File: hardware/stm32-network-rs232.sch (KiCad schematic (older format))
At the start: 57 parts, among them J1 USB, M1 Mount Hole, M2 Mount Hole, M3 Mount Hole, M4 Mount Hole, P1 BELFUSE-08B0-1X1T-06-F, P2 P10, P3 DEBUG, P4 SWD, P5 RS232-TAP, P6 RS-232-DB-9-DTE, U1 ENC28J60, U2 STM32-48PIN, U3 MAX3221, U4 MOSFET-P, X1 25MHz, X2 8MHz

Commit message: more mods
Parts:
- C25: renamed from C?; value CP -> 10uF
- gave numbers to parts that had none: 1
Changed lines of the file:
@@
 USBDM
 $Comp
-L +3.3V #PWR31
+L +3.3V #PWR35
 U 1 1 53B60338
 P 9800 3000
-F 0 "#PWR31" H 9800 3090 20  0001 C CNN
+F 0 "#PWR35" H 9800 3090 20  0001 C CNN
 F 1 "+3.3V" H 9800 3090 30  0000 C CNN
 F 2 "" H 9800 3000 60  0000 C CNN
@@
 $EndComp
 $Comp
-L GNDPWR #PWR32
+L GNDPWR #PWR36
 U 1 1 53B603BB
 P 9800 3600
-F 0 "#PWR32" H 9800 3650 40  0001 C CNN
+F 0 "#PWR36" H 9800 3650 40  0001 C CNN
 F 1 "GNDPWR" H 9800 3520 40  0001 C CNN
 F 2 "" H 9800 3600 60  0000 C CNN
@@
 $EndComp
 $Comp
-L GNDPWR #PWR36
+L GNDPWR #PWR40
 U 1 1 53B60B2A
 P 10500 3800
-F 0 "#PWR36" H 10500 3850 40  0001 C CNN
+F 0 "#PWR40" H 10500 3850 40  0001 C CNN
 F 1 "GNDPWR" H 10500 3720 40  0001 C CNN
 F 2 "" H 10500 3800 60  0000 C CNN
@@
 $EndComp
 $Comp
-L GNDPWR #PWR37
+L GNDPWR #PWR41
 U 1 1 53B60B43
 P 10700 3800
-F 0 "#PWR37" H 10700 3850 40  0001 C CNN
+F 0 "#PWR41" H 10700 3850 40  0001 C CNN
 F 1 "GNDPWR" H 10700 3720 40  0001 C CNN
 F 2 "" H 10700 3800 60  0000 C CNN
@@
 $EndComp
 $Comp
-L +3.3V #PWR35
+L +3.3V #PWR39
 U 1 1 53B613AF
 P 10500 2100
-F 0 "#PWR35" H 10500 2190 20  0001 C CNN
+F 0 "#PWR39" H 10500 2190 20  0001 C CNN
 F 1 "+3.3V" H 10500 2190 30  0000 C CNN
 F 2 "" H 10500 2100 60  0000 C CNN
@@
 $EndComp
 $Comp
-L +3.3V #PWR34
+L +3.3V #PWR38
 U 1 1 53B6163A
 P 10100 2100
-F 0 "#PWR34" H 10100 2190 20  0001 C CNN
+F 0 "#PWR38" H 10100 2190 20  0001 C CNN
 F 1 "+3.3V" H 10100 2190 30  0000 C CNN
 F 2 "" H 10100 2100 60  0000 C CNN
@@
 USART1TX
 $Comp
-L GNDPWR #PWR25
+L GNDPWR #PWR29
 U 1 1 53B62BA7
 P 8000 1600
-F 0 "#PWR25" H 8000 1650 40  0001 C CNN
+F 0 "#PWR29" H 8000 1650 40  0001 C CNN
 F 1 "GNDPWR" H 8000 1520 40  0001 C CNN
 F 2 "" H 8000 1600 60  0000 C CNN
@@
 $EndComp
 $Comp
-L GNDPWR #PWR27
+L GNDPWR #PWR31
 U 1 1 53B63110
 P 8000 2800
-F 0 "#PWR27" H 8000 2850 40  0001 C CNN
+F 0 "#PWR31" H 8000 2850 40  0001 C CNN
 F 1 "GNDPWR" H 8000 2720 40  0001 C CNN
 F 2 "" H 8000 2800 60  0000 C CNN
@@
 $EndComp
 $Comp
-L +3.3V #PWR26
+L +3.3V #PWR30
 U 1 1 53B63160
 P 8000 1900
-F 0 "#PWR26" H 8000 1990 20  0001 C CNN
+F 0 "#PWR30" H 8000 1990 20  0001 C CNN
 F 1 "+3.3V" H 8000 1990 30  0000 C CNN
 F 2 "" H 8000 1900 60  0000 C CNN
@@
 $EndComp
 $Comp
-L GNDPWR #PWR33
+L GNDPWR #PWR37
 U 1 1 53B6399D
 P 9900 1600
-F 0 "#PWR33" H 9900 1650 40  0001 C CNN
+F 0 "#PWR37" H 9900 1650 40  0001 C CNN
 F 1 "GNDPWR" H 9900 1520 40  0001 C CNN
 F 2 "" H 9900 1600 60  0000 C CNN
@@
 $EndComp
 $Comp
-L GNDPWR #PWR24
+L GNDPWR #PWR28
 U 1 1 53B803A1
 P 7500 5600
-F 0 "#PWR24" H 7500 5650 40  0001 C CNN
+F 0 "#PWR28" H 7500 5650 40  0001 C CNN
 F 1 "GNDPWR" H 7500 5520 40  0001 C CNN
 F 2 "" H 7500 5600 60  0000 C CNN
@@
 $EndComp
 $Comp
-L GNDPWR #PWR23
+L GNDPWR #PWR27
 U 1 1 53B806FF
 P 7200 5600
-F 0 "#PWR23" H 7200 5650 40  0001 C CNN
+F 0 "#PWR27" H 7200 5650 40  0001 C CNN
 F 1 "GNDPWR" H 7200 5520 40  0001 C CNN
 F 2 "" H 7200 5600 60  0000 C CNN
@@
 $EndComp
 $Comp
-L GNDPWR #PWR21
+L GNDPWR #PWR25
 U 1 1 53B80C7E
 P 6900 5600
-F 0 "#PWR21" H 6900 5650 40  0001 C CNN
+F 0 "#PWR25" H 6900 5650 40  0001 C CNN
 F 1 "GNDPWR" H 6900 5520 40  0001 C CNN
 F 2 "" H 6900 5600 60  0000 C CNN
@@
 $EndComp
 $Comp
-L +3.3V #PWR22
+L +3.3V #PWR26
 U 1 1 53B80DCA
 P 7200 3200
-F 0 "#PWR22" H 7200 3290 20  0001 C CNN
+F 0 "#PWR26" H 7200 3290 20  0001 C CNN
 F 1 "+3.3V" H 7200 3290 30  0000 C CNN
 F 2 "" H 7200 3200 60  0000 C CNN
@@
 	9200 4700 9800 4700
 $Comp
-L GNDPWR #PWR30
+L GNDPWR #PWR34
 U 1 1 53B8429D
 P 9700 5600
-F 0 "#PWR30" H 9700 5650 40  0001 C CNN
+F 0 "#PWR34" H 9700 5650 40  0001 C CNN
 F 1 "GNDPWR" H 9700 5520 40  0001 C CNN
 F 2 "" H 9700 5600 60  0000 C CNN
@@
 $EndComp
 $Comp
-L GNDPWR #PWR29
+L GNDPWR #PWR33
 U 1 1 53B8524D
 P 8300 6100
-F 0 "#PWR29" H 8300 6150 40  0001 C CNN
+F 0 "#PWR33" H 8300 6150 40  0001 C CNN
 F 1 "GNDPWR" H 8300 6020 40  0001 C CNN
 F 2 "" H 8300 6100 60  0000 C CNN
@@
 $EndComp
 $Comp
-L +3.3V #PWR28
+L +3.3V #PWR32
 U 1 1 53B852CF
 P 8300 5700
-F 0 "#PWR28" H 8300 5790 20  0001 C CNN
+F 0 "#PWR32" H 8300 5790 20  0001 C CNN
 F 1 "+3.3V" H 8300 5790 30  0000 C CNN
 F 2 "" H 8300 5700 60  0000 C CNN
@@
 $EndComp
 $Comp
-L +3.3V #PWR17
+L +3.3V #PWR19
 U 1 1 53B84CAE
 P 6000 2900
-F 0 "#PWR17" H 6000 2990 20  0001 C CNN
+F 0 "#PWR19" H 6000 2990 20  0001 C CNN
 F 1 "+3.3V" H 6000 2990 30  0000 C CNN
 F 2 "" H 6000 2900 60  0000 C CNN
@@
 	6000 3000 6000 2900
 $Comp
-L GNDPWR #PWR18
+L GNDPWR #PWR20
 U 1 1 53B84DDA
 P 6000 4300
-F 0 "#PWR18" H 6000 4350 40  0001 C CNN
+F 0 "#PWR20" H 6000 4350 40  0001 C CNN
 F 1 "GNDPWR" H 6000 4220 40  0001 C CNN
 F 2 "" H 6000 4300 60  0000 C CNN
@@
 $EndComp
 $Comp
-L GNDPWR #PWR20
+L GNDPWR #PWR24
 U 1 1 53B85CCD
 P 6500 1600
-F 0 "#PWR20" H 6500 1650 40  0001 C CNN
+F 0 "#PWR24" H 6500 1650 40  0001 C CNN
 F 1 "GNDPWR" H 6500 1520 40  0001 C CNN
 F 2 "" H 6500 1600 60  0000 C CNN
@@
 $EndComp
 $Comp
-L +3.3V #PWR19
+L +3.3V #PWR23
 U 1 1 53B85DD1
 P 6500 900
-F 0 "#PWR19" H 6500 990 20  0001 C CNN
+F 0 "#PWR23" H 6500 990 20  0001 C CNN
 F 1 "+3.3V" H 6500 990 30  0000 C CNN
 F 2 "" H 6500 900 60  0000 C CNN
@@
 	4100 6400 4100 6700
 $Comp
-L GNDPWR #PWR16
+L GNDPWR #PWR17
 U 1 1 53B85B11
 P 4800 7300
-F 0 "#PWR16" H 4800 7350 40  0001 C CNN
+F 0 "#PWR17" H 4800 7350 40  0001 C CNN
 F 1 "GNDPWR" H 4800 7220 40  0001 C CNN
 F 2 "" H 4800 7300 60  0000 C CNN
@@
 	4400 7400 3400 7400
 $Comp
-L VREG_VOUTCENTER U?
+L VREG_VOUTCENTER U5
 U 1 1 53B990D6
 P 5400 4950
-F 0 "U?" H 5550 4754 60  0000 C CNN
+F 0 "U5" H 5550 4754 60  0000 C CNN
 F 1 "ZLDO1117" H 5400 5150 60  0000 C CNN
 F 2 "" H 5400 4950 60  0000 C CNN
@@
 $EndComp
 $Comp
-L +5V #PWR?
+L +5V #PWR16
 U 1 1 53B991D9
 P 4800 4700
-F 0 "#PWR?" H 4800 4790 20  0001 C CNN
+F 0 "#PWR16" H 4800 4790 20  0001 C CNN
 F 1 "+5V" H 4800 4790 30  0000 C CNN
 F 2 "" H 4800 4700 60  0000 C CNN
@@
 NoConn ~ 5800 5000
 $Comp
-L GNDPWR #PWR?
+L GNDPWR #PWR18
 U 1 1 53B9949C
 P 5400 5300
-F 0 "#PWR?" H 5400 5350 40  0001 C CNN
+F 0 "#PWR18" H 5400 5350 40  0001 C CNN
 F 1 "GNDPWR" H 5400 5220 40  0001 C CNN
 F 2 "" H 5400 5300 60  0000 C CNN
@@
 	5400 5200 5400 5300
 $Comp
-L +3.3V #PWR?
+L +3.3V #PWR22
 U 1 1 53B99624
 P 6300 4700
-F 0 "#PWR?" H 6300 4790 20  0001 C CNN
+F 0 "#PWR22" H 6300 4790 20  0001 C CNN
 F 1 "+3.3V" H 6300 4790 30  0000 C CNN
 F 2 "" H 6300 4700 60  0000 C CNN
@@
 	6300 4900 6300 4700
 $Comp
-L CP C?
+L CP C25
 U 1 1 53B9986A
 P 6100 5100
-F 0 "C?" H 6125 5150 30  0000 L CNN
-F 1 "CP" H 6125 5050 30  0000 L CNN
+F 0 "C25" H 6125 5150 30  0000 L CNN
+F 1 "10uF" H 6125 5050 30  0000 L CNN
 F 2 "" H 6100 5100 60  0000 C CNN
 F 3 "" H 6100 5100 60  0000 C CNN
@@
 $EndComp
 $Comp
-L GNDPWR #PWR?
+L GNDPWR #PWR21
 U 1 1 53B998C4
 P 6100 5300
-F 0 "#PWR?" H 6100 5350 40  0001 C CNN
+F 0 "#PWR21" H 6100 5350 40  0001 C CNN
 F 1 "GNDPWR" H 6100 5220 40  0001 C CNN
 F 2 "" H 6100 5300 60  0000 C CNN

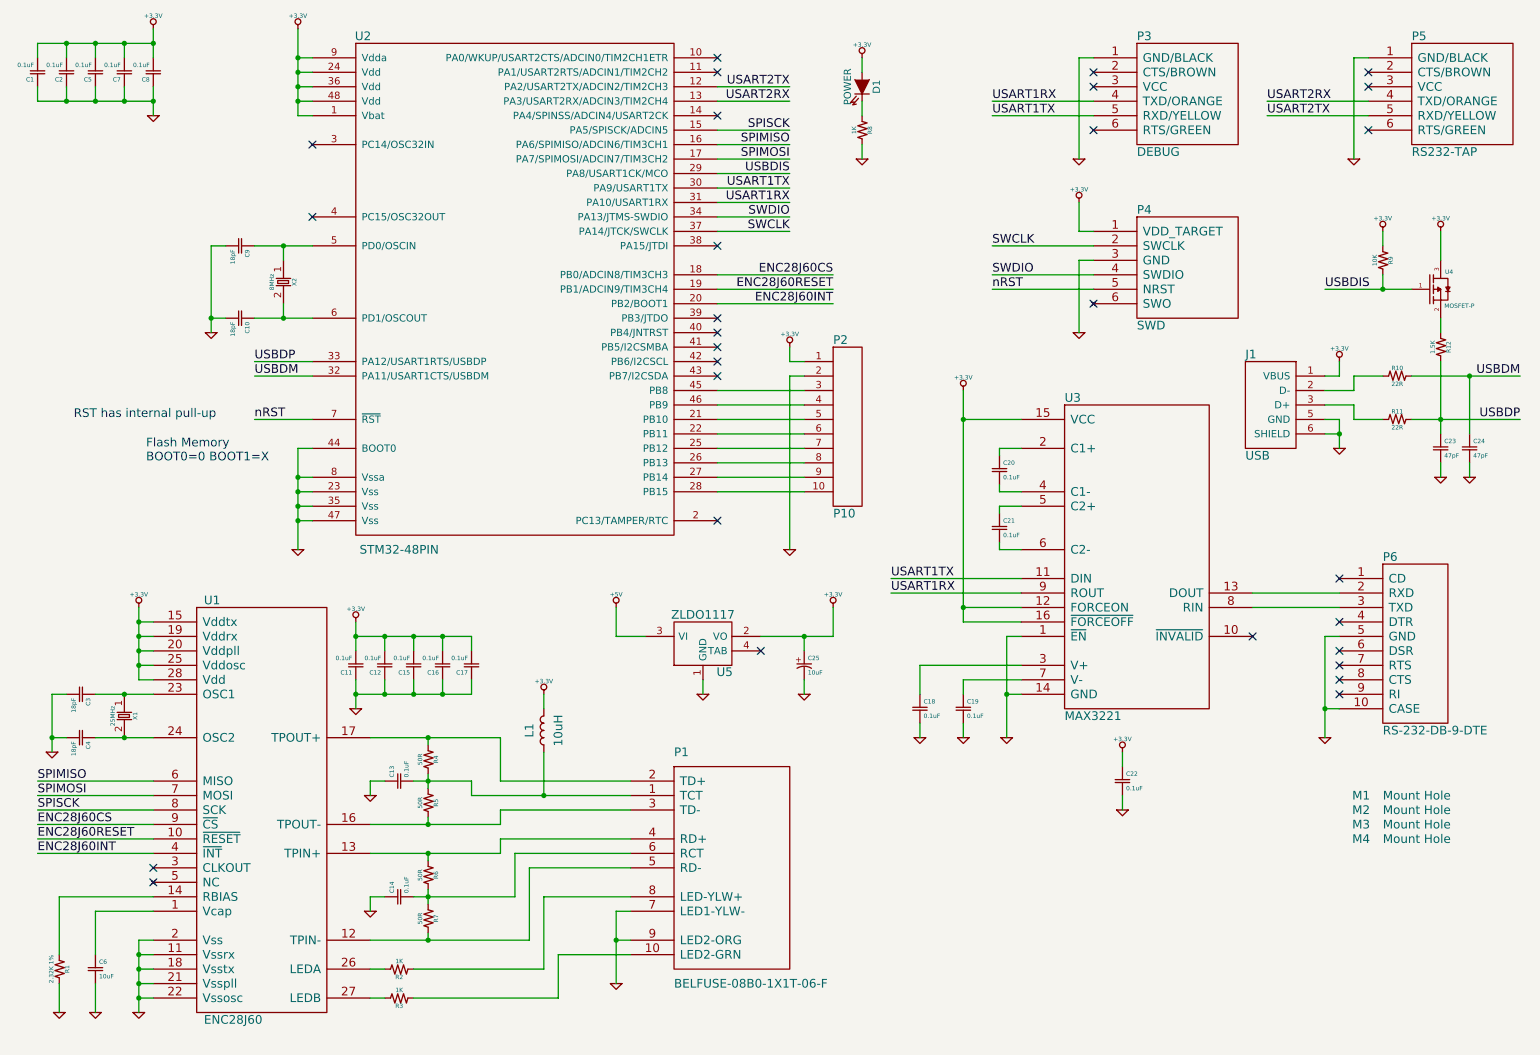
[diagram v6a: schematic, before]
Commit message: add rx/tx toggles
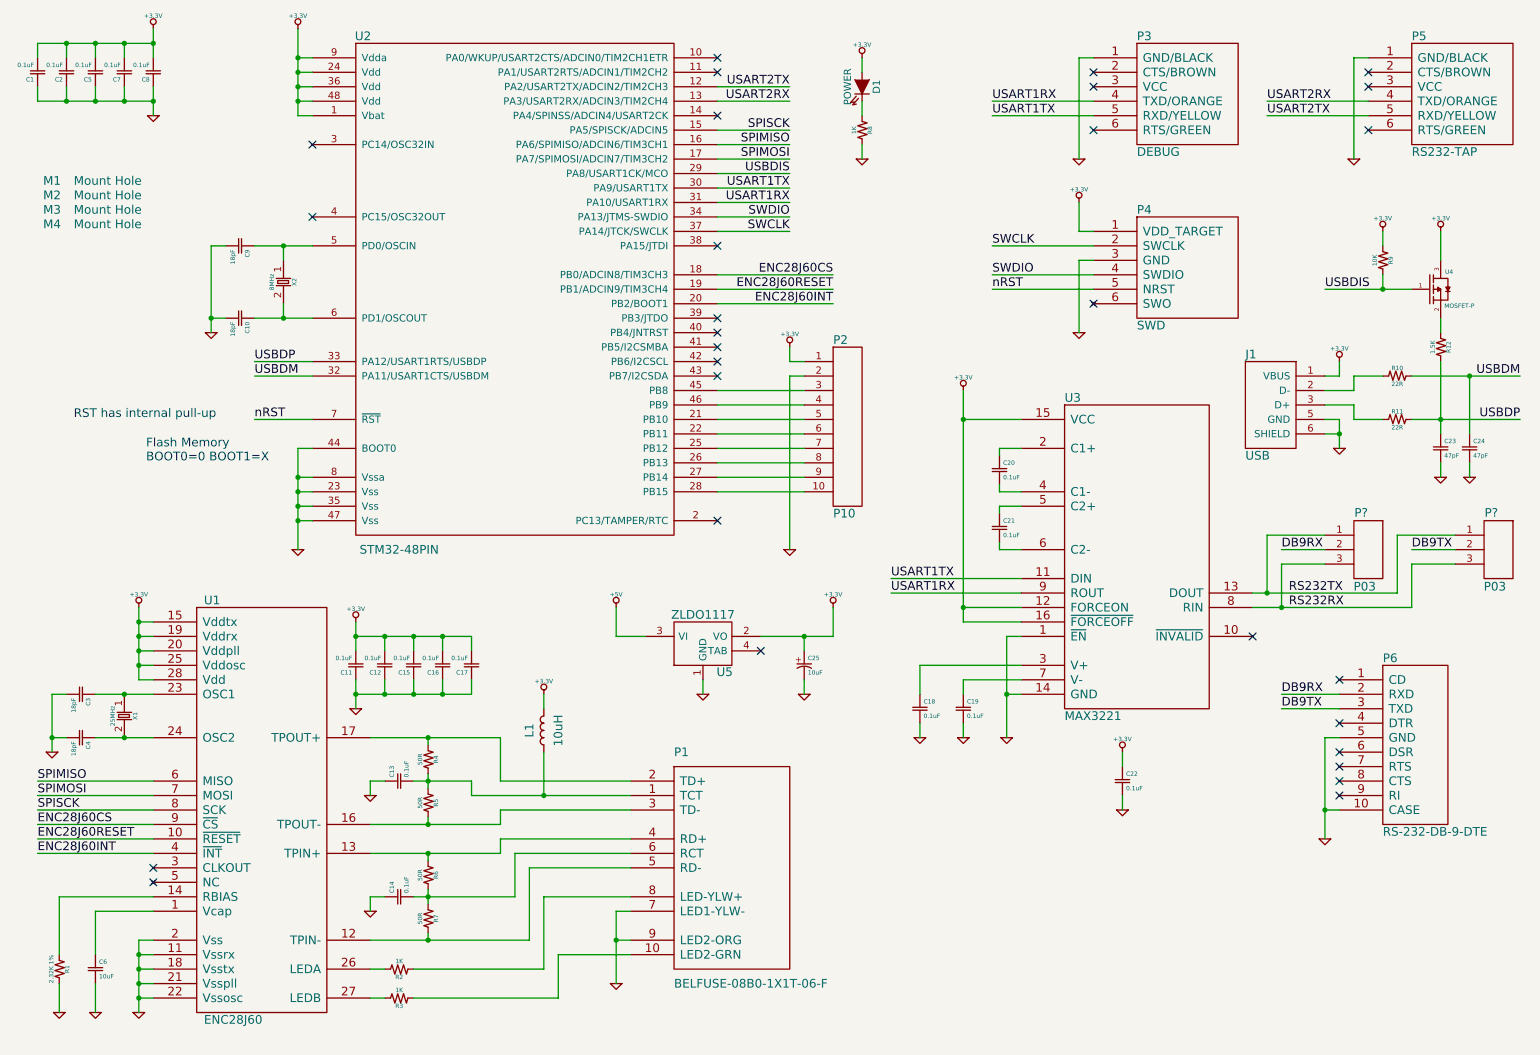
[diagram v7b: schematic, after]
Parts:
- added P? (x2): P03, symbol P03
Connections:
- net DB9RX: now reaches P6.2 (RXD)
- net DB9RX: now also P?.2; no longer U3.13 (DOUT)
- net DB9TX: now reaches P6.3 (TXD)
- net DB9TX: now also P?.2; no longer U3.8 (RIN)
- new net RS232RX: P?.3, P?.3, U3.8 (RIN)
- new net RS232TX: P?.1, P?.1, U3.13 (DOUT)
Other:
- moved on the sheet: P6
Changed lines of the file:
@@
 L MECH M1
 U 1 1 53B60D6B
-P 9900 6000
-F 0 "M1" H 9950 6000 60  0000 C CNN
-F 1 "Mount Hole" H 10100 6000 60  0000 L CNN
-F 2 "" H 9900 6000 60  0000 C CNN
-F 3 "" H 9900 6000 60  0000 C CNN
-	1    9900 6000
+P 850 1750
+F 0 "M1" H 900 1750 60  0000 C CNN
+F 1 "Mount Hole" H 1050 1750 60  0000 L CNN
+F 2 "" H 850 1750 60  0000 C CNN
+F 3 "" H 850 1750 60  0000 C CNN
+	1    850  1750
 	1    0    0    -1
 $EndComp
@@
 L MECH M2
 U 1 1 53B60F6A
-P 9900 6100
-F 0 "M2" H 9950 6100 60  0000 C CNN
-F 1 "Mount Hole" H 10100 6100 60  0000 L CNN
-F 2 "" H 9900 6100 60  0000 C CNN
-F 3 "" H 9900 6100 60  0000 C CNN
-	1    9900 6100
+P 850 1850
+F 0 "M2" H 900 1850 60  0000 C CNN
+F 1 "Mount Hole" H 1050 1850 60  0000 L CNN
+F 2 "" H 850 1850 60  0000 C CNN
+F 3 "" H 850 1850 60  0000 C CNN
+	1    850  1850
 	1    0    0    -1
 $EndComp
@@
 L MECH M3
 U 1 1 53B60F93
-P 9900 6200
-F 0 "M3" H 9950 6200 60  0000 C CNN
-F 1 "Mount Hole" H 10100 6200 60  0000 L CNN
-F 2 "" H 9900 6200 60  0000 C CNN
-F 3 "" H 9900 6200 60  0000 C CNN
-	1    9900 6200
+P 850 1950
+F 0 "M3" H 900 1950 60  0000 C CNN
+F 1 "Mount Hole" H 1050 1950 60  0000 L CNN
+F 2 "" H 850 1950 60  0000 C CNN
+F 3 "" H 850 1950 60  0000 C CNN
+	1    850  1950
 	1    0    0    -1
 $EndComp
@@
 L MECH M4
 U 1 1 53B60FB9
-P 9900 6300
-F 0 "M4" H 9950 6300 60  0000 C CNN
-F 1 "Mount Hole" H 10100 6300 60  0000 L CNN
-F 2 "" H 9900 6300 60  0000 C CNN
-F 3 "" H 9900 6300 60  0000 C CNN
-	1    9900 6300
+P 850 2050
+F 0 "M4" H 900 2050 60  0000 C CNN
+F 1 "Mount Hole" H 1050 2050 60  0000 L CNN
+F 2 "" H 850 2050 60  0000 C CNN
+F 3 "" H 850 2050 60  0000 C CNN
+	1    850  2050
 	1    0    0    -1
 $EndComp
@@
 L RS-232-DB-9-DTE P6
 U 1 1 53B8374E
-P 10300 4900
-F 0 "P6" H 10100 5450 60  0000 L CNN
-F 1 "RS-232-DB-9-DTE" H 10100 4250 60  0000 L CNN
-F 2 "" H 10100 4300 60  0000 C CNN
-F 3 "" H 10100 4300 60  0000 C CNN
-	1    10300 4900
-	1    0    0    -1
-$EndComp
-Wire Wire Line
-	9200 4600 9800 4600
-Wire Wire Line
-	9200 4700 9800 4700
+P 10300 5600
+F 0 "P6" H 10100 6150 60  0000 L CNN
+F 1 "RS-232-DB-9-DTE" H 10100 4950 60  0000 L CNN
+F 2 "" H 10100 5000 60  0000 C CNN
+F 3 "" H 10100 5000 60  0000 C CNN
+	1    10300 5600
+	1    0    0    -1
+$EndComp
 $Comp
 L GNDPWR #PWR34
 U 1 1 53B8429D
-P 9700 5600
-F 0 "#PWR34" H 9700 5650 40  0001 C CNN
-F 1 "GNDPWR" H 9700 5520 40  0001 C CNN
-F 2 "" H 9700 5600 60  0000 C CNN
-F 3 "" H 9700 5600 60  0000 C CNN
-	1    9700 5600
-	1    0    0    -1
-$EndComp
-Wire Wire Line
-	9800 4900 9700 4900
-Wire Wire Line
-	9700 4900 9700 5600
-Wire Wire Line
-	9800 5400 9700 5400
-Connection ~ 9700 5400
-NoConn ~ 9800 4500
-NoConn ~ 9800 5300
-NoConn ~ 9800 4800
-NoConn ~ 9800 5000
-NoConn ~ 9800 5100
+P 9700 6300
+F 0 "#PWR34" H 9700 6350 40  0001 C CNN
+F 1 "GNDPWR" H 9700 6220 40  0001 C CNN
+F 2 "" H 9700 6300 60  0000 C CNN
+F 3 "" H 9700 6300 60  0000 C CNN
+	1    9700 6300
+	1    0    0    -1
+$EndComp
+Wire Wire Line
+	9800 5600 9700 5600
+Wire Wire Line
+	9700 5600 9700 6300
+Wire Wire Line
+	9800 6100 9700 6100
+Connection ~ 9700 6100
 NoConn ~ 9800 5200
+NoConn ~ 9800 6000
+NoConn ~ 9800 5500
+NoConn ~ 9800 5700
+NoConn ~ 9800 5800
+NoConn ~ 9800 5900
 $Comp
 L C C22
@@
 Wire Wire Line
 	6100 5200 6100 5300
+$Comp
+L P03 P?
+U 1 1 53BA93FC
+P 10800 4100
+F 0 "P?" H 10850 4155 60  0000 C CNN
+F 1 "P03" H 10875 3645 60  0000 C CNN
+F 2 "" H 10800 4100 60  0000 C CNN
+F 3 "" H 10800 4100 60  0000 C CNN
+	1    10800 4100
+	1    0    0    -1
+$EndComp
+$Comp
+L P03 P?
+U 1 1 53BA9CCF
+P 9900 4100
+F 0 "P?" H 9950 4155 60  0000 C CNN
+F 1 "P03" H 9975 3645 60  0000 C CNN
+F 2 "" H 9900 4100 60  0000 C CNN
+F 3 "" H 9900 4100 60  0000 C CNN
+	1    9900 4100
+	1    0    0    -1
+$EndComp
+Wire Wire Line
+	9200 4600 10200 4600
+Wire Wire Line
+	9300 4600 9300 4200
+Wire Wire Line
+	9300 4200 9700 4200
+Wire Wire Line
+	9200 4700 10300 4700
+Wire Wire Line
+	9400 4700 9400 4400
+Wire Wire Line
+	9400 4400 9700 4400
+Wire Wire Line
+	10200 4600 10200 4200
+Wire Wire Line
+	10200 4200 10600 4200
+Connection ~ 9300 4600
+Wire Wire Line
+	10300 4700 10300 4400
+Wire Wire Line
+	10300 4400 10600 4400
+Connection ~ 9400 4700
+Text Label 9400 4300 0    60   ~ 0
+DB9RX
+Text Label 10300 4300 0    60   ~ 0
+DB9TX
+Wire Wire Line
+	9400 4300 9700 4300
+Wire Wire Line
+	10300 4300 10600 4300
+Wire Wire Line
+	9800 5300 9400 5300
+Wire Wire Line
+	9800 5400 9400 5400
+Text Label 9400 5300 0    60   ~ 0
+DB9RX
+Text Label 9400 5400 0    60   ~ 0
+DB9TX
+Text Label 9450 4600 0    60   ~ 0
+RS232TX
+Text Label 9450 4700 0    60   ~ 0
+RS232RX
 $EndSCHEMATC

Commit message: more modules
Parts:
- gave numbers to parts that had none: 2
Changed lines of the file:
@@
 	6100 5200 6100 5300
 $Comp
-L P03 P?
+L P03 P8
 U 1 1 53BA93FC
 P 10800 4100
-F 0 "P?" H 10850 4155 60  0000 C CNN
+F 0 "P8" H 10850 4155 60  0000 C CNN
 F 1 "P03" H 10875 3645 60  0000 C CNN
 F 2 "" H 10800 4100 60  0000 C CNN
@@
 $EndComp
 $Comp
-L P03 P?
+L P03 P7
 U 1 1 53BA9CCF
 P 9900 4100
-F 0 "P?" H 9950 4155 60  0000 C CNN
+F 0 "P7" H 9950 4155 60  0000 C CNN
 F 1 "P03" H 9975 3645 60  0000 C CNN
 F 2 "" H 9900 4100 60  0000 C CNN
